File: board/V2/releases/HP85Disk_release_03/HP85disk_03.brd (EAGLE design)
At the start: 100 x 75 mm, 105 parts, among them J1 POWER_JACKSUPER_BOMB_DIGITY, J3 503398-1892, J4 USB_MINI-B_SMT, Q1 BSS138DW-7-F, U1 ATMEGA1284P-AUR, U10 MIC5205, U11 MAX811LEUS+T, U2 TPIC6A596DWRG4, U3 SN75ALS162DWR, U4 75ALS160, U6 SN74LVC1G32DCKR, U7 FT232RL, U8 TXS0104EDR, U9 LM1117, Y2 20MHz

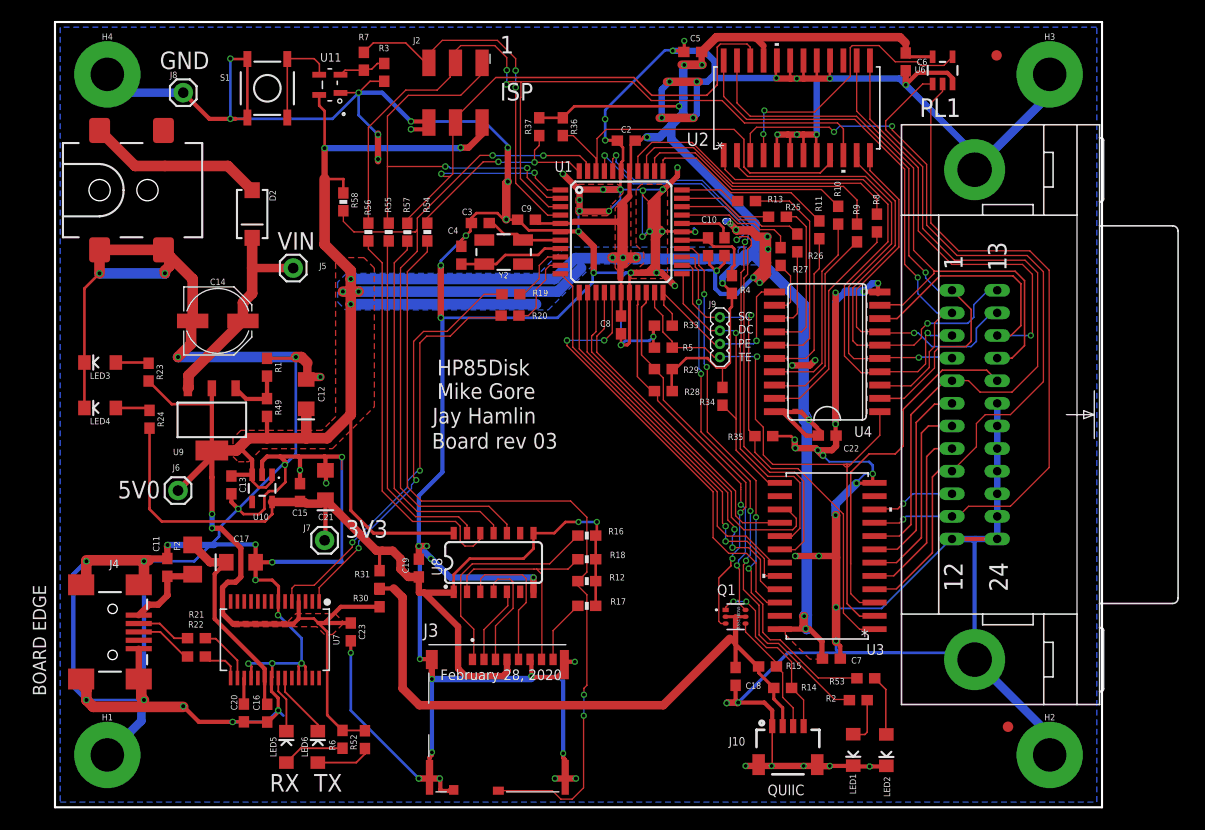
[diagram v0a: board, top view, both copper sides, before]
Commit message: Added RTC DS1703 - page 2 U5
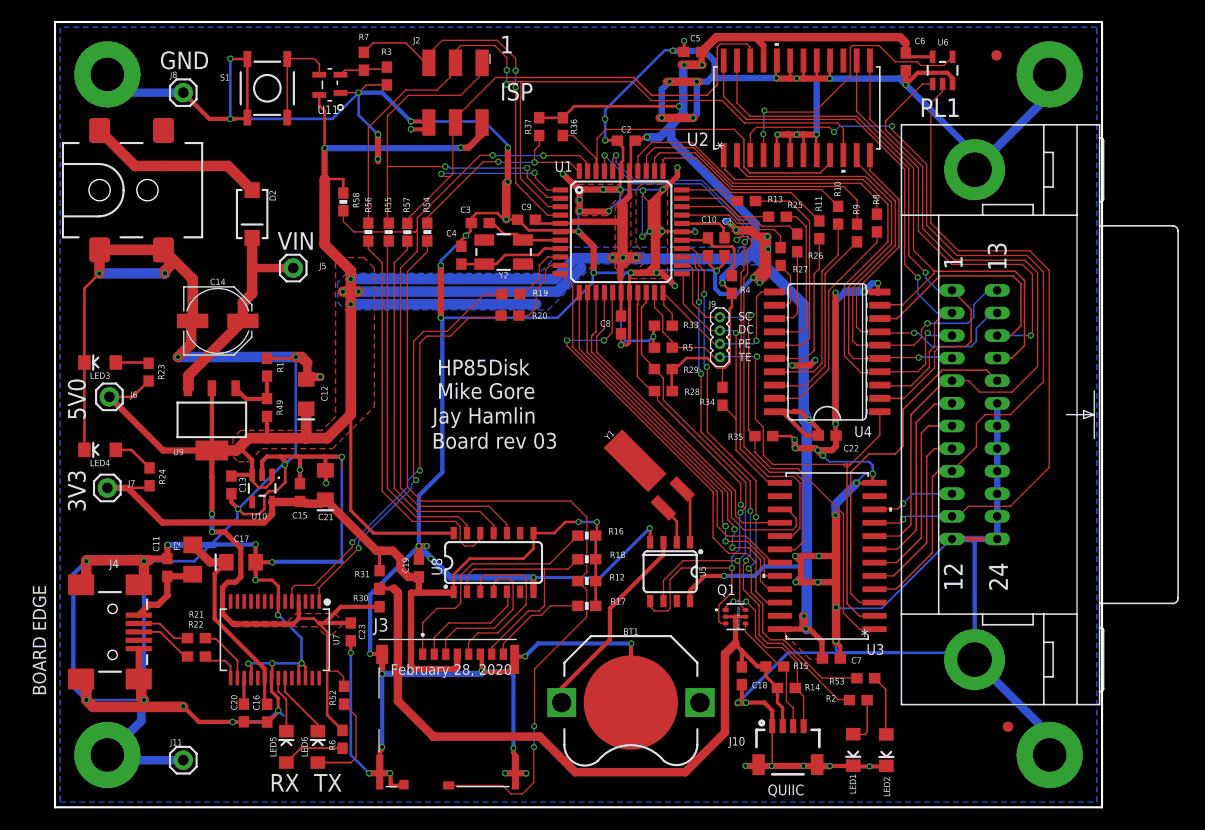
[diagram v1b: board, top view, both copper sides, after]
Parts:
- added BT1: (no value), SparkFun-Batteries:BATTCON_12MM_PTH
- added J11: (no value), SparkFun-Connectors:1X01
- added U5: DS1307Z, SparkFun-Clocks:SO08-0.15
- added Y1: 32.768kHz, SparkFun-Clocks:CRYSTAL-SMD-2X6-CYL
- moved J7 21.3 mm to (5.00, 30.5)
- moved J6 11.1 mm to (5.20, 39.2)
- moved R24 5.50 mm to (9.03, 31.6)
- moved J3 4.78 mm to (37.5, 9.00)
- moved R52 4.70 mm to (27.6, 10.7)
- moved LED4 4.00 mm to (4.31, 34.1)
- moved R15 0.70 mm to (68.8, 13.4)
- moved C18 0.60 mm to (65.6, 12.6)
- moved R3 0.43 mm to (31.7, 69.8)
- moved R14 0.35 mm to (69.8, 11.4)
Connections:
- new net N$16: U5.1, Y1.X2
- new net N$17: BT1.VCC@1, U5.3
- new net N$18: U5.2, Y1.X1
- net 5V: now also U5.8
- net 5V_SCL: now also U5.6
- net 5V_SDA: now also U5.5
- net GND: now also BT1.GND, J11.1, U5.4
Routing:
- net GND: track 974.2 -> 1021.4 mm, vias 120 -> 124
- net N$17: track 0.00 -> 19.3 mm
- net 5V: track 441.8 -> 460.1 mm, vias 19 -> 20
- net 5V_SDA: track 37.7 -> 49.5 mm
- net I2C_VDDIO: track 63.1 -> 73.2 mm
- net 5V_SCL: track 35.7 -> 45.5 mm
- net 3.3V: track 92.5 -> 87.0 mm
- net N$16: track 0.00 -> 5.41 mm
- net N$5: track 5.35 -> 9.93 mm
- net N$18: track 0.00 -> 3.83 mm
- net SD_CS: track 7.44 -> 11.2 mm
- net SD_MOSI: track 11.0 -> 14.6 mm
- net N$11: track 6.10 -> 9.62 mm
- net SD_CLK: track 13.9 -> 16.5 mm
- net SD_MISO: track 21.6 -> 23.7 mm
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
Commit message: changed SDcard SPI bufffers to 74ACT125 and 74LVC125
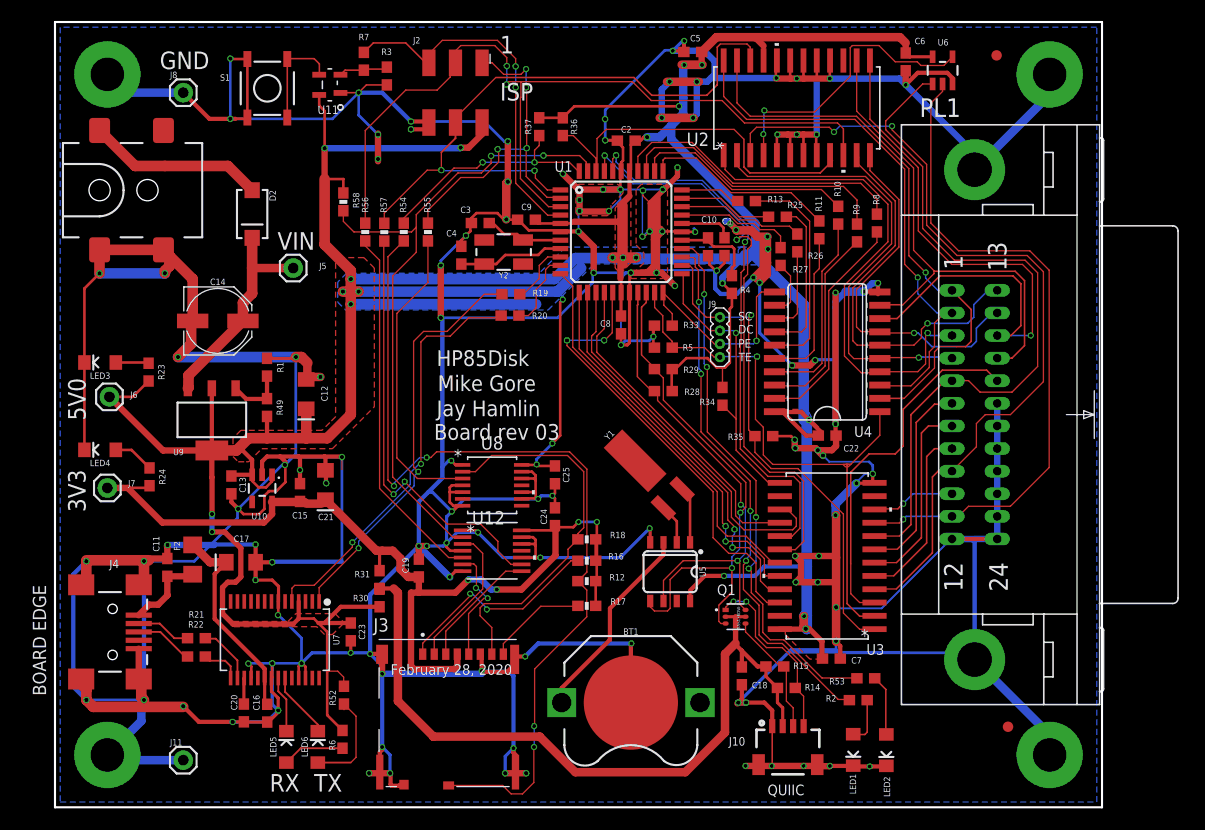
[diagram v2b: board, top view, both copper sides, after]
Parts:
- added C24, C25: 0.1uF, SparkFun-Capacitors:0603
- added U12: SN74LVC125APWR, JaysOWL_Library:PW14
- U8: value TXS0104EDR -> MC74ACT125DTR2G; device SparkFun-DigitalIC:SO14 -> JaysOWL_Library:TSSOP14_4P50X5P10
- moved U8 7.37 mm to (41.8, 30.8)
- moved R55 3.75 mm to (35.6, 54.9)
- moved R16 2.40 mm to (50.8, 23.6)
- moved R54 2.25 mm to (33.3, 54.9)
- moved R57 2.20 mm to (31.4, 54.9)
- moved R18 1.90 mm to (50.8, 25.6)
- moved R56 0.30 mm to (29.6, 54.9)
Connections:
- net 3.3V: now also C24.1, U12.14; no longer U8.1, U8.8
- net 5V: now also C25.1
- net CLK_5V0: now also U12.5; no longer U8.12
- net GND: now also C24.2, C25.2, U12.1, U12.10, U12.12, U12.13, U12.4, U12.7, U8.1, U8.10, U8.12, U8.13, U8.4, U8.5, U8.9
- net MISO_5V: now also U8.3; no longer U8.13
- net MOSI_5V0: now also U12.9; no longer U8.11
- net PB3_CS: now also U12.2; no longer U8.10
- net SD_CLK: now also U12.6; no longer U8.3
- net SD_CS: now also U12.3; no longer U8.5
- net SD_MOSI: now also U12.8; no longer U8.4
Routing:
- net GND: track 1021.4 -> 1102.1 mm, vias 124 -> 130
- net SD_MISO: track 23.7 -> 37.0 mm
- net 3.3V: track 87.0 -> 94.9 mm, vias 2 -> 4
- net SD_CD: track 80.0 -> 86.9 mm, vias 2 -> 4
- net MISO: track 40.3 -> 34.3 mm, vias 2 -> 4
- net MOSI_5V0: track 35.9 -> 41.3 mm, vias 0 -> 2
- net SD_CLK: track 16.5 -> 11.4 mm, vias 0 -> 2
- net MISO_5V: track 33.5 -> 29.1 mm
- net PB3_CS: track 67.3 -> 63.8 mm
- net CLK_5V0: track 37.7 -> 34.9 mm
- net SD_MOSI: track 14.6 -> 11.8 mm
- net SD_CS: track 11.2 -> 13.8 mm
- net N$13: track 22.8 -> 20.5 mm, vias 0 -> 2
- net PB4_CD: track 20.4 -> 22.5 mm
- net 5V: track 460.1 -> 461.2 mm, vias 20 -> 23
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
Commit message: fixed SDCArd pullups. set ftdi series R to 120R. board cleaanup
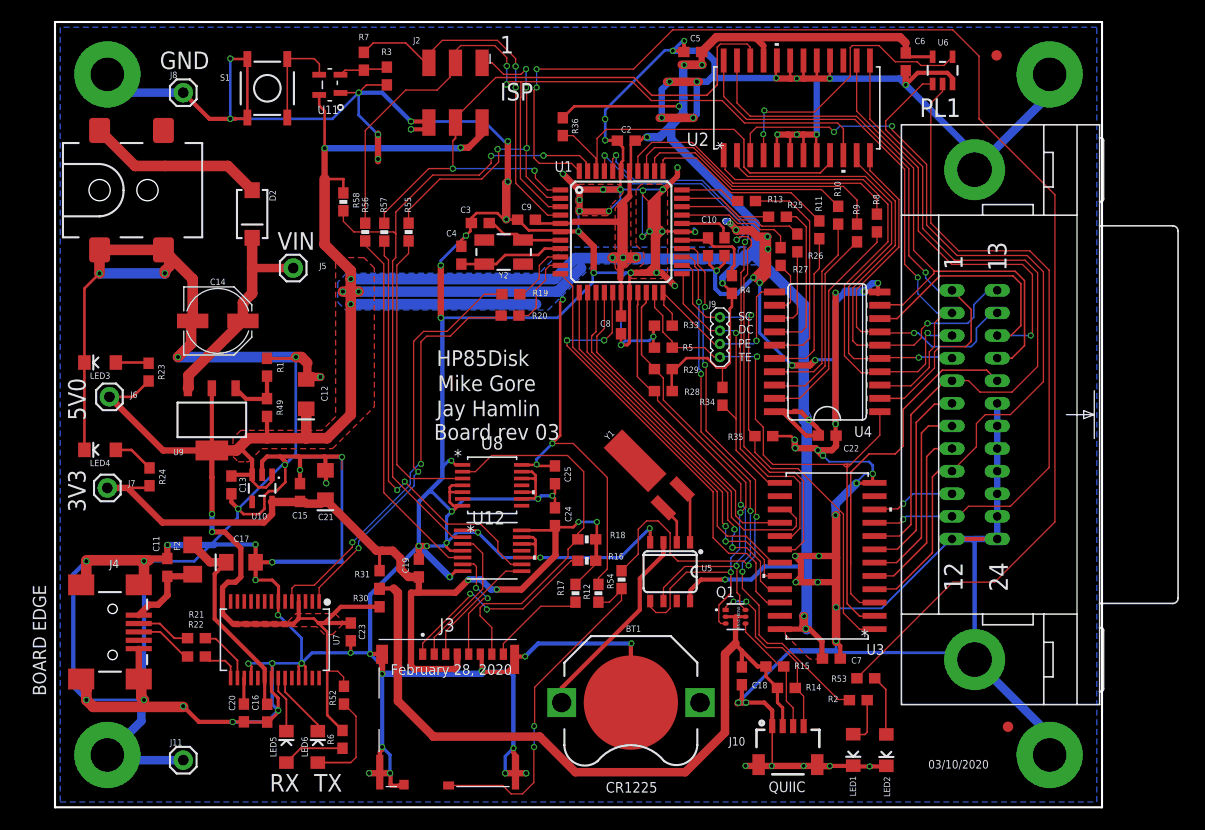
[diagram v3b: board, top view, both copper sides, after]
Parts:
- removed R37: 10K, SparkFun-Resistors:0603
- R19, R20: value 1k -> 120R
- moved R54 39.2 mm to (54.1, 21.7)
- moved R55 1.85 mm to (33.8, 54.9)
- moved R17 1.61 mm to (49.7, 20.4), turned to 90 degrees
- moved R12 1.61 mm to (51.9, 20.4), turned to 90 degrees
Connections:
- removed net PB4_CD: R37.1, R54.2, U1.44
- new net PC7_CD: R54.2, U1.26
- net 3.3V: no longer R12.2
- net 5V: now also R12.2; no longer R37.2
- net N$10: now also U1.44; no longer U1.26
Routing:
- net N$10: track 51.8 -> 131.1 mm, vias 4 -> 2
- net PC7_CD: track 0.00 -> 53.5 mm, vias 0 -> 4
- net SD_CD: track 86.9 -> 34.5 mm, vias 4 -> 2
- net PB4_CD: track 22.5 -> 0.00 mm, vias 2 -> 0
- net 5V: track 461.2 -> 476.1 mm
- net 3.3V: track 94.9 -> 91.6 mm
- net MISO: track 34.3 -> 36.2 mm
- net MOSI_5V0: track 41.3 -> 40.4 mm
- net PB3_CS: track 63.8 -> 63.1 mm
- net 5V_SCL: track 45.5 -> 44.8 mm
- net 5V_SDA: track 49.5 -> 48.9 mm
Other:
- board text added: "03/10/2020"
- board text added: "CR1225"

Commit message: released versions of board files
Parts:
- R24: value 240 -> 240R
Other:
- board text added: "03/09/2020"
- board text added: "uSD"
- board text removed: "03/10/2020"
- board text removed: "February 28, 2020"
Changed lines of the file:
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@@
 <wire x1="0" y1="0" x2="0" y2="75" width="0.2032" layer="20"/>
 <wire x1="100" y1="0" x2="100" y2="75" width="0.2032" layer="20"/>
-<text x="36.2" y="35.1" size="1.5" layer="21">Board rev 03</text>
-<text x="36.55" y="39.75" size="1.5" layer="21">Mike Gore</text>
-<text x="36.45" y="37.35" size="1.5" layer="21">Jay Hamlin</text>
+<text x="36.6" y="36.4" size="1.5" layer="21">Board rev 03</text>
+<text x="36.55" y="40.8" size="1.5" layer="21">Mike Gore</text>
+<text x="36.55" y="38.65" size="1.5" layer="21">Jay Hamlin</text>
 <text x="1.25" y="41" size="1.6764" layer="21" rot="R270">5V0</text>
 <text x="1.25" y="32.25" size="1.6764" layer="21" rot="R270">3V3</text>
@@
 <text x="24.75" y="1.5" size="1.6764" layer="21">TX</text>
 <text x="20.5" y="1.5" size="1.6764" layer="21">RX</text>
-<text x="36.45" y="42.15" size="1.5" layer="21">HP85Disk</text>
+<text x="36.6" y="43.25" size="1.5" layer="21">HP85Disk</text>
 <text x="68.15" y="1.45" size="1.016" layer="21">QUIIC</text>
-<text x="32.05" y="12.65" size="1.016" layer="21">February 28, 2020</text>
 <text x="65.3" y="42.6" size="0.8128" layer="21">TE</text>
 <text x="65.25" y="43.9" size="0.8128" layer="21">PE</text>
 <text x="65.25" y="45.25" size="0.8128" layer="21">DC</text>
 <text x="65.25" y="46.5" size="0.8128" layer="21">SC</text>
-<text x="83.4" y="3.7" size="0.8128" layer="21">03/10/2020</text>
+<text x="83.4" y="3.7" size="0.8128" layer="21">03/09/2020</text>
 <text x="52.6" y="1.4" size="1.016" layer="21">CR1225</text>
+<text x="36.35" y="4.05" size="1.016" layer="21">uSD</text>
 </plain>
 <attributes>
@@
 <attribute name="VALUE" x="4.31" y="43.4325" size="0.6096" layer="27" font="vector" ratio="20" rot="R180" align="top-center"/>
 </element>
-<element name="R24" library="SparkFun-Resistors" package="0603" value="240" x="9.03" y="31.56" smashed="yes" rot="R270">
+<element name="R24" library="SparkFun-Resistors" package="0603" value="240R" x="9.03" y="31.56" smashed="yes" rot="R270">
 <attribute name="NAME" x="9.942" y="31.56" size="0.6096" layer="25" font="vector" ratio="10" rot="R270" align="bottom-center"/>
 <attribute name="PROD_ID" value="RES-07857" x="15.38" y="31.56" size="1.778" layer="27" rot="R270" display="off"/>

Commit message: updated pcb. rotated micro SD socket. updated gerbers
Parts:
- U10: value MIC5205 -> LP5907MFX-3.3
- moved R17 22.2 mm to (29.2, 12.0)
- moved R54 3.98 mm to (50.8, 19.5), turned to 0 degrees
- moved R12 1.53 mm to (50.8, 21.5), turned to 0 degrees
- moved J3 1.50 mm to (37.6, 7.50), turned to 180 degrees
- moved J1 0.51 mm to (3.75, 58.9)
- moved J4 0.50 mm to (5.00, 16.8)
- moved PL1 0.47 mm to (88.3, 37.5)
- moved R52 0.45 mm to (27.1, 10.7)
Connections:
- net N$3 renamed XT1
- net N$4 renamed XT2
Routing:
- net SD_CLK: track 11.4 -> 36.5 mm
- net SD_MISO: track 37.0 -> 57.2 mm
- net GND: track 1101.9 -> 1082.1 mm, vias 130 -> 128
- net 3.3V: track 91.6 -> 110.8 mm, vias 4 -> 6
- net SD_CD: track 34.5 -> 16.6 mm
- net SD_CS: track 13.8 -> 30.9 mm, vias 0 -> 2
- net SD_MOSI: track 11.8 -> 27.9 mm, vias 0 -> 2
- net I2C_VDDIO: track 73.2 -> 58.3 mm, vias 0 -> 4
- net N$13: track 20.5 -> 27.3 mm, vias 2 -> 0
- net N$11: track 9.53 -> 14.6 mm
- net PC7_CD: track 53.5 -> 57.1 mm
- net 5V: track 476.1 -> 474.5 mm
- net GPIB_D7: track 62.0 -> 61.0 mm
- net GPIB_IFC: track 80.5 -> 81.5 mm
- net GPIB_D2: track 52.0 -> 53.0 mm
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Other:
- board text added: "03/15/2020"
- board text added: "Board rev 03b"
- board text removed: "03/09/2020"
- board text removed: "Board rev 03"
